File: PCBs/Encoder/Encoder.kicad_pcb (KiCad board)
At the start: 2 copper layers, 6 x 25 mm, 3 parts, among them J1 Conn_01x06_Male, U1 AS5047D

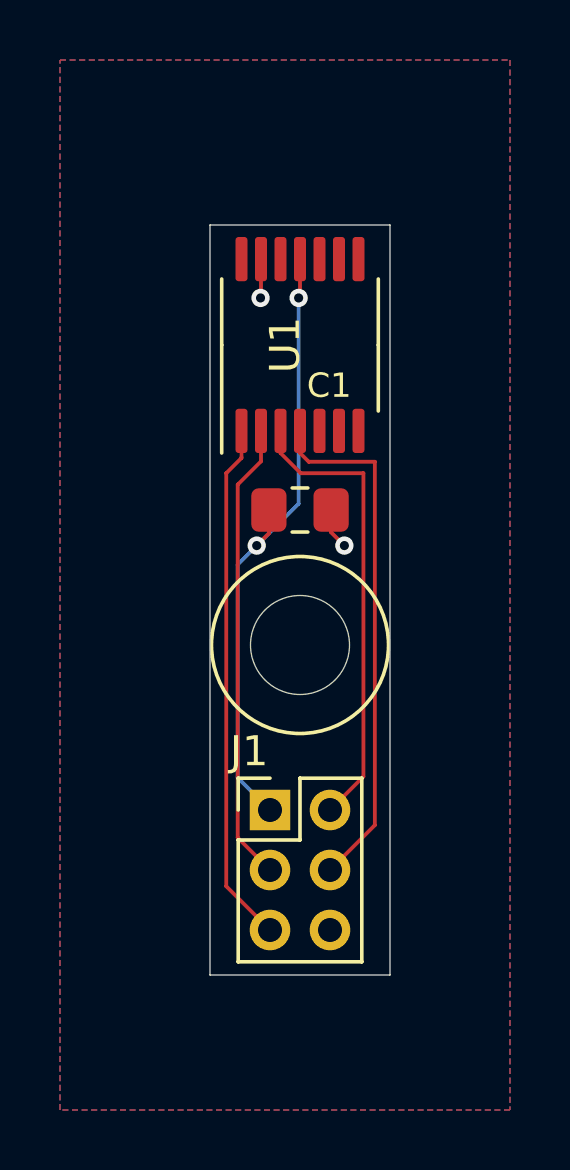
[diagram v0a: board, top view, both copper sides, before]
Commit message: J0 stls
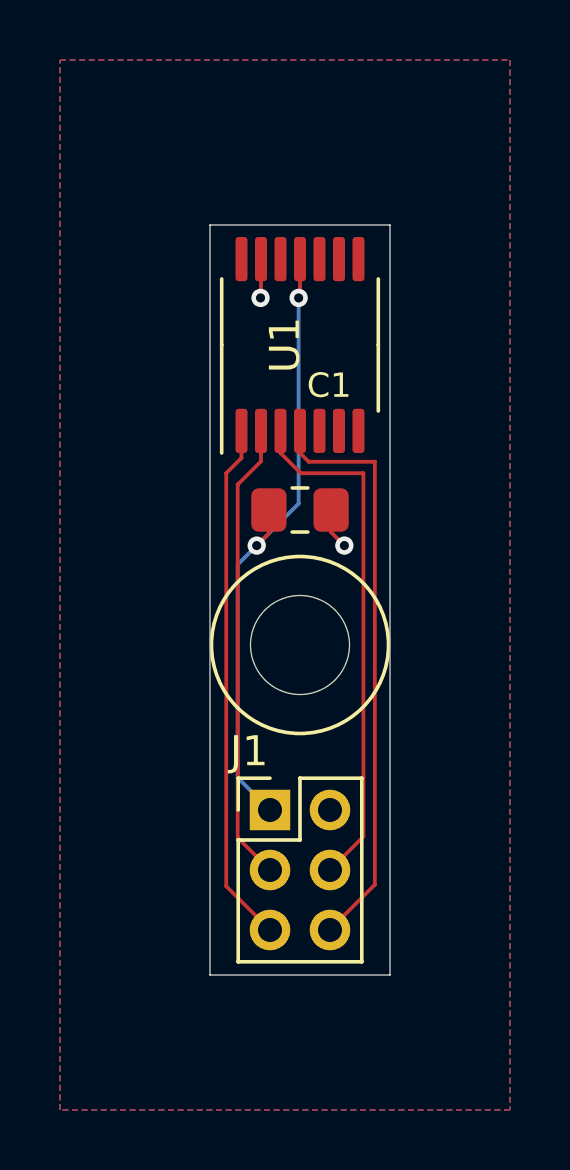
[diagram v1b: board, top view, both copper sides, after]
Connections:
- J1 pad 2: MISO -> GND
- J1 pad 4: MOSI -> MISO
- J1 pad 6: GND -> MOSI
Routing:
- net MISO: track 15.5 -> 17.5 mm
- net MOSI: track 17.6 -> 19.6 mm
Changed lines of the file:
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@@
-(kicad_pcb (version 20171130) (host pcbnew "(5.1.9)-1")
+(kicad_pcb (version 20171130) (host pcbnew "(5.1.10)-1")
   (general
     (thickness 1.6)
     (drawings 12)
-    (tracks 35)
+    (tracks 36)
     (zones 0)
     (modules 3)
@@
       (effects (font (size 1 1) (thickness 0.15)))
     )
+    (fp_line (start 0 -1) (end 3 -1) (layer F.Fab) (width 0.1))
+    (fp_line (start 3 -1) (end 3 5) (layer F.Fab) (width 0.1))
+    (fp_line (start 3 5) (end -1 5) (layer F.Fab) (width 0.1))
+    (fp_line (start -1 5) (end -1 0) (layer F.Fab) (width 0.1))
+    (fp_line (start -1 0) (end 0 -1) (layer F.Fab) (width 0.1))
+    (fp_line (start -1.06 5.06) (end 3.06 5.06) (layer F.SilkS) (width 0.12))
+    (fp_line (start -1.06 1) (end -1.06 5.06) (layer F.SilkS) (width 0.12))
+    (fp_line (start 3.06 -1.06) (end 3.06 5.06) (layer F.SilkS) (width 0.12))
+    (fp_line (start -1.06 1) (end 1 1) (layer F.SilkS) (width 0.12))
+    (fp_line (start 1 1) (end 1 -1.06) (layer F.SilkS) (width 0.12))
+    (fp_line (start 1 -1.06) (end 3.06 -1.06) (layer F.SilkS) (width 0.12))
+    (fp_line (start -1.06 0) (end -1.06 -1.06) (layer F.SilkS) (width 0.12))
+    (fp_line (start -1.06 -1.06) (end 0 -1.06) (layer F.SilkS) (width 0.12))
+    (fp_line (start -1.5 -1.5) (end -1.5 5.5) (layer F.CrtYd) (width 0.05))
+    (fp_line (start -1.5 5.5) (end 3.5 5.5) (layer F.CrtYd) (width 0.05))
+    (fp_line (start 3.5 5.5) (end 3.5 -1.5) (layer F.CrtYd) (width 0.05))
     (fp_line (start 3.5 -1.5) (end -1.5 -1.5) (layer F.CrtYd) (width 0.05))
-    (fp_line (start 3.5 5.5) (end 3.5 -1.5) (layer F.CrtYd) (width 0.05))
-    (fp_line (start -1.5 5.5) (end 3.5 5.5) (layer F.CrtYd) (width 0.05))
-    (fp_line (start -1.5 -1.5) (end -1.5 5.5) (layer F.CrtYd) (width 0.05))
-    (fp_line (start -1.06 -1.06) (end 0 -1.06) (layer F.SilkS) (width 0.12))
-    (fp_line (start -1.06 0) (end -1.06 -1.06) (layer F.SilkS) (width 0.12))
-    (fp_line (start 1 -1.06) (end 3.06 -1.06) (layer F.SilkS) (width 0.12))
-    (fp_line (start 1 1) (end 1 -1.06) (layer F.SilkS) (width 0.12))
-    (fp_line (start -1.06 1) (end 1 1) (layer F.SilkS) (width 0.12))
-    (fp_line (start 3.06 -1.06) (end 3.06 5.06) (layer F.SilkS) (width 0.12))
-    (fp_line (start -1.06 1) (end -1.06 5.06) (layer F.SilkS) (width 0.12))
-    (fp_line (start -1.06 5.06) (end 3.06 5.06) (layer F.SilkS) (width 0.12))
-    (fp_line (start -1 0) (end 0 -1) (layer F.Fab) (width 0.1))
-    (fp_line (start -1 5) (end -1 0) (layer F.Fab) (width 0.1))
-    (fp_line (start 3 5) (end -1 5) (layer F.Fab) (width 0.1))
-    (fp_line (start 3 -1) (end 3 5) (layer F.Fab) (width 0.1))
-    (fp_line (start 0 -1) (end 3 -1) (layer F.Fab) (width 0.1))
     (fp_text user %R (at 1 2 90) (layer F.Fab)
       (effects (font (size 1 1) (thickness 0.15)))
     )
     (pad 6 thru_hole oval (at 2 4) (size 1.35 1.35) (drill 0.8) (layers *.Cu *.Mask)
-      (net 1 GND))
+      (net 6 MOSI))
     (pad 5 thru_hole oval (at 0 4) (size 1.35 1.35) (drill 0.8) (layers *.Cu *.Mask)
       (net 3 CS))
     (pad 4 thru_hole oval (at 2 2) (size 1.35 1.35) (drill 0.8) (layers *.Cu *.Mask)
-      (net 6 MOSI))
+      (net 5 MISO))
     (pad 3 thru_hole oval (at 0 2) (size 1.35 1.35) (drill 0.8) (layers *.Cu *.Mask)
       (net 4 CLK))
     (pad 2 thru_hole oval (at 2 0) (size 1.35 1.35) (drill 0.8) (layers *.Cu *.Mask)
-      (net 5 MISO))
+      (net 1 GND))
     (pad 1 thru_hole rect (at 0 0) (size 1.35 1.35) (drill 0.8) (layers *.Cu *.Mask)
       (net 2 +3V3))
@@
       (effects (font (size 1 1) (thickness 0.15)))
     )
+    (fp_line (start 0 2.61) (end 2.2 2.61) (layer F.SilkS) (width 0.12))
+    (fp_line (start 0 2.61) (end -2.2 2.61) (layer F.SilkS) (width 0.12))
+    (fp_line (start 0 -2.61) (end 2.2 -2.61) (layer F.SilkS) (width 0.12))
+    (fp_line (start 0 -2.61) (end -3.6 -2.61) (layer F.SilkS) (width 0.12))
+    (fp_line (start -1.2 -2.5) (end 2.2 -2.5) (layer F.Fab) (width 0.1))
+    (fp_line (start 2.2 -2.5) (end 2.2 2.5) (layer F.Fab) (width 0.1))
+    (fp_line (start 2.2 2.5) (end -2.2 2.5) (layer F.Fab) (width 0.1))
+    (fp_line (start -2.2 2.5) (end -2.2 -1.5) (layer F.Fab) (width 0.1))
+    (fp_line (start -2.2 -1.5) (end -1.2 -2.5) (layer F.Fab) (width 0.1))
+    (fp_line (start -3.85 -2.75) (end -3.85 2.75) (layer F.CrtYd) (width 0.05))
+    (fp_line (start -3.85 2.75) (end 3.85 2.75) (layer F.CrtYd) (width 0.05))
+    (fp_line (start 3.85 2.75) (end 3.85 -2.75) (layer F.CrtYd) (width 0.05))
     (fp_line (start 3.85 -2.75) (end -3.85 -2.75) (layer F.CrtYd) (width 0.05))
-    (fp_line (start 3.85 2.75) (end 3.85 -2.75) (layer F.CrtYd) (width 0.05))
-    (fp_line (start -3.85 2.75) (end 3.85 2.75) (layer F.CrtYd) (width 0.05))
-    (fp_line (start -3.85 -2.75) (end -3.85 2.75) (layer F.CrtYd) (width 0.05))
-    (fp_line (start -2.2 -1.5) (end -1.2 -2.5) (layer F.Fab) (width 0.1))
-    (fp_line (start -2.2 2.5) (end -2.2 -1.5) (layer F.Fab) (width 0.1))
-    (fp_line (start 2.2 2.5) (end -2.2 2.5) (layer F.Fab) (width 0.1))
-    (fp_line (start 2.2 -2.5) (end 2.2 2.5) (layer F.Fab) (width 0.1))
-    (fp_line (start -1.2 -2.5) (end 2.2 -2.5) (layer F.Fab) (width 0.1))
-    (fp_line (start 0 -2.61) (end -3.6 -2.61) (layer F.SilkS) (width 0.12))
-    (fp_line (start 0 -2.61) (end 2.2 -2.61) (layer F.SilkS) (width 0.12))
-    (fp_line (start 0 2.61) (end -2.2 2.61) (layer F.SilkS) (width 0.12))
-    (fp_line (start 0 2.61) (end 2.2 2.61) (layer F.SilkS) (width 0.12))
     (fp_text user %R (at 0 0 90) (layer F.Fab)
       (effects (font (size 1 1) (thickness 0.15)))
@@
       (effects (font (size 1 1) (thickness 0.15)))
     )
+    (fp_line (start -1 0.625) (end -1 -0.625) (layer F.Fab) (width 0.1))
+    (fp_line (start -1 -0.625) (end 1 -0.625) (layer F.Fab) (width 0.1))
+    (fp_line (start 1 -0.625) (end 1 0.625) (layer F.Fab) (width 0.1))
+    (fp_line (start 1 0.625) (end -1 0.625) (layer F.Fab) (width 0.1))
+    (fp_line (start -0.261252 -0.735) (end 0.261252 -0.735) (layer F.SilkS) (width 0.12))
+    (fp_line (start -0.261252 0.735) (end 0.261252 0.735) (layer F.SilkS) (width 0.12))
+    (fp_line (start -1.88 0.98) (end -1.88 -0.98) (layer F.CrtYd) (width 0.05))
+    (fp_line (start -1.88 -0.98) (end 1.88 -0.98) (layer F.CrtYd) (width 0.05))
+    (fp_line (start 1.88 -0.98) (end 1.88 0.98) (layer F.CrtYd) (width 0.05))
     (fp_line (start 1.88 0.98) (end -1.88 0.98) (layer F.CrtYd) (width 0.05))
-    (fp_line (start 1.88 -0.98) (end 1.88 0.98) (layer F.CrtYd) (width 0.05))
-    (fp_line (start -1.88 -0.98) (end 1.88 -0.98) (layer F.CrtYd) (width 0.05))
-    (fp_line (start -1.88 0.98) (end -1.88 -0.98) (layer F.CrtYd) (width 0.05))
-    (fp_line (start -0.261252 0.735) (end 0.261252 0.735) (layer F.SilkS) (width 0.12))
-    (fp_line (start -0.261252 -0.735) (end 0.261252 -0.735) (layer F.SilkS) (width 0.12))
-    (fp_line (start 1 0.625) (end -1 0.625) (layer F.Fab) (width 0.1))
-    (fp_line (start 1 -0.625) (end 1 0.625) (layer F.Fab) (width 0.1))
-    (fp_line (start -1 -0.625) (end 1 -0.625) (layer F.Fab) (width 0.1))
-    (fp_line (start -1 0.625) (end -1 -0.625) (layer F.Fab) (width 0.1))
     (fp_text user %R (at 0 0) (layer F.Fab)
       (effects (font (size 0.5 0.5) (thickness 0.08)))
@@
   (segment (start 148.023 88.773) (end 150.114 88.773) (width 0.127) (layer F.Cu) (net 5))
   (segment (start 147.35 88.1) (end 148.023 88.773) (width 0.127) (layer F.Cu) (net 5))
-  (segment (start 150.114 98.886) (end 149 100) (width 0.127) (layer F.Cu) (net 5))
   (segment (start 147.35 87.3625) (end 147.35 88.1) (width 0.127) (layer F.Cu) (net 5))
-  (segment (start 150.495 100.505) (end 149 102) (width 0.127) (layer F.Cu) (net 6))
-  (segment (start 150.495 88.392) (end 150.495 100.505) (width 0.127) (layer F.Cu) (net 6))
+  (segment (start 150.114 100.886) (end 149 102) (width 0.127) (layer F.Cu) (net 5))
+  (segment (start 150.114 98.886) (end 150.114 100.886) (width 0.127) (layer F.Cu) (net 5))
+  (segment (start 150.495 102.489) (end 149 103.984) (width 0.127) (layer F.Cu) (net 6))
+  (segment (start 150.495 88.392) (end 150.495 102.489) (width 0.127) (layer F.Cu) (net 6))
   (segment (start 148.292 88.392) (end 150.495 88.392) (width 0.127) (layer F.Cu) (net 6))
   (segment (start 148 88.1) (end 148.292 88.392) (width 0.127) (layer F.Cu) (net 6))

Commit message: ordered boards
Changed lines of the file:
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@@
-(kicad_pcb (version 20171130) (host pcbnew "(5.1.10)-1")
+(kicad_pcb (version 20171130) (host pcbnew "(5.1.9)-1")
   (general
     (thickness 1.6)
@@
     (pcbplotparams
       (layerselection 0x010fc_ffffffff)
-      (usegerberextensions false)
-      (usegerberattributes true)
-      (usegerberadvancedattributes true)
-      (creategerberjobfile true)
+      (usegerberextensions true)
+      (usegerberattributes false)
+      (usegerberadvancedattributes false)
+      (creategerberjobfile false)
       (excludeedgelayer true)
       (linewidth 0.100000)
@@
       (psa4output false)
       (plotreference true)
-      (plotvalue true)
+      (plotvalue false)
       (plotinvisibletext false)
       (padsonsilk false)
-      (subtractmaskfromsilk false)
+      (subtractmaskfromsilk true)
       (outputformat 1)
       (mirror false)
-      (drillshape 1)
+      (drillshape 0)
       (scaleselection 1)
-      (outputdirectory ""))
+      (outputdirectory "/Output/"))
   )
   (net 0 "")
@@
       (effects (font (size 1 1) (thickness 0.15)))
     )
+    (fp_line (start 3.5 -1.5) (end -1.5 -1.5) (layer F.CrtYd) (width 0.05))
+    (fp_line (start 3.5 5.5) (end 3.5 -1.5) (layer F.CrtYd) (width 0.05))
+    (fp_line (start -1.5 5.5) (end 3.5 5.5) (layer F.CrtYd) (width 0.05))
+    (fp_line (start -1.5 -1.5) (end -1.5 5.5) (layer F.CrtYd) (width 0.05))
+    (fp_line (start -1.06 -1.06) (end 0 -1.06) (layer F.SilkS) (width 0.12))
+    (fp_line (start -1.06 0) (end -1.06 -1.06) (layer F.SilkS) (width 0.12))
+    (fp_line (start 1 -1.06) (end 3.06 -1.06) (layer F.SilkS) (width 0.12))
+    (fp_line (start 1 1) (end 1 -1.06) (layer F.SilkS) (width 0.12))
+    (fp_line (start -1.06 1) (end 1 1) (layer F.SilkS) (width 0.12))
+    (fp_line (start 3.06 -1.06) (end 3.06 5.06) (layer F.SilkS) (width 0.12))
+    (fp_line (start -1.06 1) (end -1.06 5.06) (layer F.SilkS) (width 0.12))
+    (fp_line (start -1.06 5.06) (end 3.06 5.06) (layer F.SilkS) (width 0.12))
+    (fp_line (start -1 0) (end 0 -1) (layer F.Fab) (width 0.1))
+    (fp_line (start -1 5) (end -1 0) (layer F.Fab) (width 0.1))
+    (fp_line (start 3 5) (end -1 5) (layer F.Fab) (width 0.1))
+    (fp_line (start 3 -1) (end 3 5) (layer F.Fab) (width 0.1))
     (fp_line (start 0 -1) (end 3 -1) (layer F.Fab) (width 0.1))
-    (fp_line (start 3 -1) (end 3 5) (layer F.Fab) (width 0.1))
-    (fp_line (start 3 5) (end -1 5) (layer F.Fab) (width 0.1))
-    (fp_line (start -1 5) (end -1 0) (layer F.Fab) (width 0.1))
-    (fp_line (start -1 0) (end 0 -1) (layer F.Fab) (width 0.1))
-    (fp_line (start -1.06 5.06) (end 3.06 5.06) (layer F.SilkS) (width 0.12))
-    (fp_line (start -1.06 1) (end -1.06 5.06) (layer F.SilkS) (width 0.12))
-    (fp_line (start 3.06 -1.06) (end 3.06 5.06) (layer F.SilkS) (width 0.12))
-    (fp_line (start -1.06 1) (end 1 1) (layer F.SilkS) (width 0.12))
-    (fp_line (start 1 1) (end 1 -1.06) (layer F.SilkS) (width 0.12))
-    (fp_line (start 1 -1.06) (end 3.06 -1.06) (layer F.SilkS) (width 0.12))
-    (fp_line (start -1.06 0) (end -1.06 -1.06) (layer F.SilkS) (width 0.12))
-    (fp_line (start -1.06 -1.06) (end 0 -1.06) (layer F.SilkS) (width 0.12))
-    (fp_line (start -1.5 -1.5) (end -1.5 5.5) (layer F.CrtYd) (width 0.05))
-    (fp_line (start -1.5 5.5) (end 3.5 5.5) (layer F.CrtYd) (width 0.05))
-    (fp_line (start 3.5 5.5) (end 3.5 -1.5) (layer F.CrtYd) (width 0.05))
-    (fp_line (start 3.5 -1.5) (end -1.5 -1.5) (layer F.CrtYd) (width 0.05))
     (fp_text user %R (at 1 2 90) (layer F.Fab)
       (effects (font (size 1 1) (thickness 0.15)))
@@
       (effects (font (size 1 1) (thickness 0.15)))
     )
+    (fp_line (start 3.85 -2.75) (end -3.85 -2.75) (layer F.CrtYd) (width 0.05))
+    (fp_line (start 3.85 2.75) (end 3.85 -2.75) (layer F.CrtYd) (width 0.05))
+    (fp_line (start -3.85 2.75) (end 3.85 2.75) (layer F.CrtYd) (width 0.05))
+    (fp_line (start -3.85 -2.75) (end -3.85 2.75) (layer F.CrtYd) (width 0.05))
+    (fp_line (start -2.2 -1.5) (end -1.2 -2.5) (layer F.Fab) (width 0.1))
+    (fp_line (start -2.2 2.5) (end -2.2 -1.5) (layer F.Fab) (width 0.1))
+    (fp_line (start 2.2 2.5) (end -2.2 2.5) (layer F.Fab) (width 0.1))
+    (fp_line (start 2.2 -2.5) (end 2.2 2.5) (layer F.Fab) (width 0.1))
+    (fp_line (start -1.2 -2.5) (end 2.2 -2.5) (layer F.Fab) (width 0.1))
+    (fp_line (start 0 -2.61) (end -3.6 -2.61) (layer F.SilkS) (width 0.12))
+    (fp_line (start 0 -2.61) (end 2.2 -2.61) (layer F.SilkS) (width 0.12))
+    (fp_line (start 0 2.61) (end -2.2 2.61) (layer F.SilkS) (width 0.12))
     (fp_line (start 0 2.61) (end 2.2 2.61) (layer F.SilkS) (width 0.12))
-    (fp_line (start 0 2.61) (end -2.2 2.61) (layer F.SilkS) (width 0.12))
-    (fp_line (start 0 -2.61) (end 2.2 -2.61) (layer F.SilkS) (width 0.12))
-    (fp_line (start 0 -2.61) (end -3.6 -2.61) (layer F.SilkS) (width 0.12))
-    (fp_line (start -1.2 -2.5) (end 2.2 -2.5) (layer F.Fab) (width 0.1))
-    (fp_line (start 2.2 -2.5) (end 2.2 2.5) (layer F.Fab) (width 0.1))
-    (fp_line (start 2.2 2.5) (end -2.2 2.5) (layer F.Fab) (width 0.1))
-    (fp_line (start -2.2 2.5) (end -2.2 -1.5) (layer F.Fab) (width 0.1))
-    (fp_line (start -2.2 -1.5) (end -1.2 -2.5) (layer F.Fab) (width 0.1))
-    (fp_line (start -3.85 -2.75) (end -3.85 2.75) (layer F.CrtYd) (width 0.05))
-    (fp_line (start -3.85 2.75) (end 3.85 2.75) (layer F.CrtYd) (width 0.05))
-    (fp_line (start 3.85 2.75) (end 3.85 -2.75) (layer F.CrtYd) (width 0.05))
-    (fp_line (start 3.85 -2.75) (end -3.85 -2.75) (layer F.CrtYd) (width 0.05))
     (fp_text user %R (at 0 0 90) (layer F.Fab)
       (effects (font (size 1 1) (thickness 0.15)))
@@
       (effects (font (size 1 1) (thickness 0.15)))
     )
+    (fp_line (start 1.88 0.98) (end -1.88 0.98) (layer F.CrtYd) (width 0.05))
+    (fp_line (start 1.88 -0.98) (end 1.88 0.98) (layer F.CrtYd) (width 0.05))
+    (fp_line (start -1.88 -0.98) (end 1.88 -0.98) (layer F.CrtYd) (width 0.05))
+    (fp_line (start -1.88 0.98) (end -1.88 -0.98) (layer F.CrtYd) (width 0.05))
+    (fp_line (start -0.261252 0.735) (end 0.261252 0.735) (layer F.SilkS) (width 0.12))
+    (fp_line (start -0.261252 -0.735) (end 0.261252 -0.735) (layer F.SilkS) (width 0.12))
+    (fp_line (start 1 0.625) (end -1 0.625) (layer F.Fab) (width 0.1))
+    (fp_line (start 1 -0.625) (end 1 0.625) (layer F.Fab) (width 0.1))
+    (fp_line (start -1 -0.625) (end 1 -0.625) (layer F.Fab) (width 0.1))
     (fp_line (start -1 0.625) (end -1 -0.625) (layer F.Fab) (width 0.1))
-    (fp_line (start -1 -0.625) (end 1 -0.625) (layer F.Fab) (width 0.1))
-    (fp_line (start 1 -0.625) (end 1 0.625) (layer F.Fab) (width 0.1))
-    (fp_line (start 1 0.625) (end -1 0.625) (layer F.Fab) (width 0.1))
-    (fp_line (start -0.261252 -0.735) (end 0.261252 -0.735) (layer F.SilkS) (width 0.12))
-    (fp_line (start -0.261252 0.735) (end 0.261252 0.735) (layer F.SilkS) (width 0.12))
-    (fp_line (start -1.88 0.98) (end -1.88 -0.98) (layer F.CrtYd) (width 0.05))
-    (fp_line (start -1.88 -0.98) (end 1.88 -0.98) (layer F.CrtYd) (width 0.05))
-    (fp_line (start 1.88 -0.98) (end 1.88 0.98) (layer F.CrtYd) (width 0.05))
-    (fp_line (start 1.88 0.98) (end -1.88 0.98) (layer F.CrtYd) (width 0.05))
     (fp_text user %R (at 0 0) (layer F.Fab)
       (effects (font (size 0.5 0.5) (thickness 0.08)))
     )
-    (pad 2 smd roundrect (at 1.0375 0) (size 1.175 1.45) (layers F.Cu F.Paste F.Mask) (roundrect_rratio 0.212766)
+    (pad 2 smd roundrect (at 1.0375 0) (size 1.175 1.45) (layers F.Cu F.Paste F.Mask) (roundrect_rratio 0.2127659574468085)
       (net 1 GND))
-    (pad 1 smd roundrect (at -1.0375 0) (size 1.175 1.45) (layers F.Cu F.Paste F.Mask) (roundrect_rratio 0.212766)
+    (pad 1 smd roundrect (at -1.0375 0) (size 1.175 1.45) (layers F.Cu F.Paste F.Mask) (roundrect_rratio 0.2127659574468085)
       (net 2 +3V3))
     (model ${KISYS3DMOD}/Capacitor_SMD.3dshapes/C_0805_2012Metric.wrl
